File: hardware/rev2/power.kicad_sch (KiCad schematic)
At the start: 20 parts, among them U5 MP2664GG-xxxx-P, U6 TPS63805YFFR, U7 MAX17055ETB+

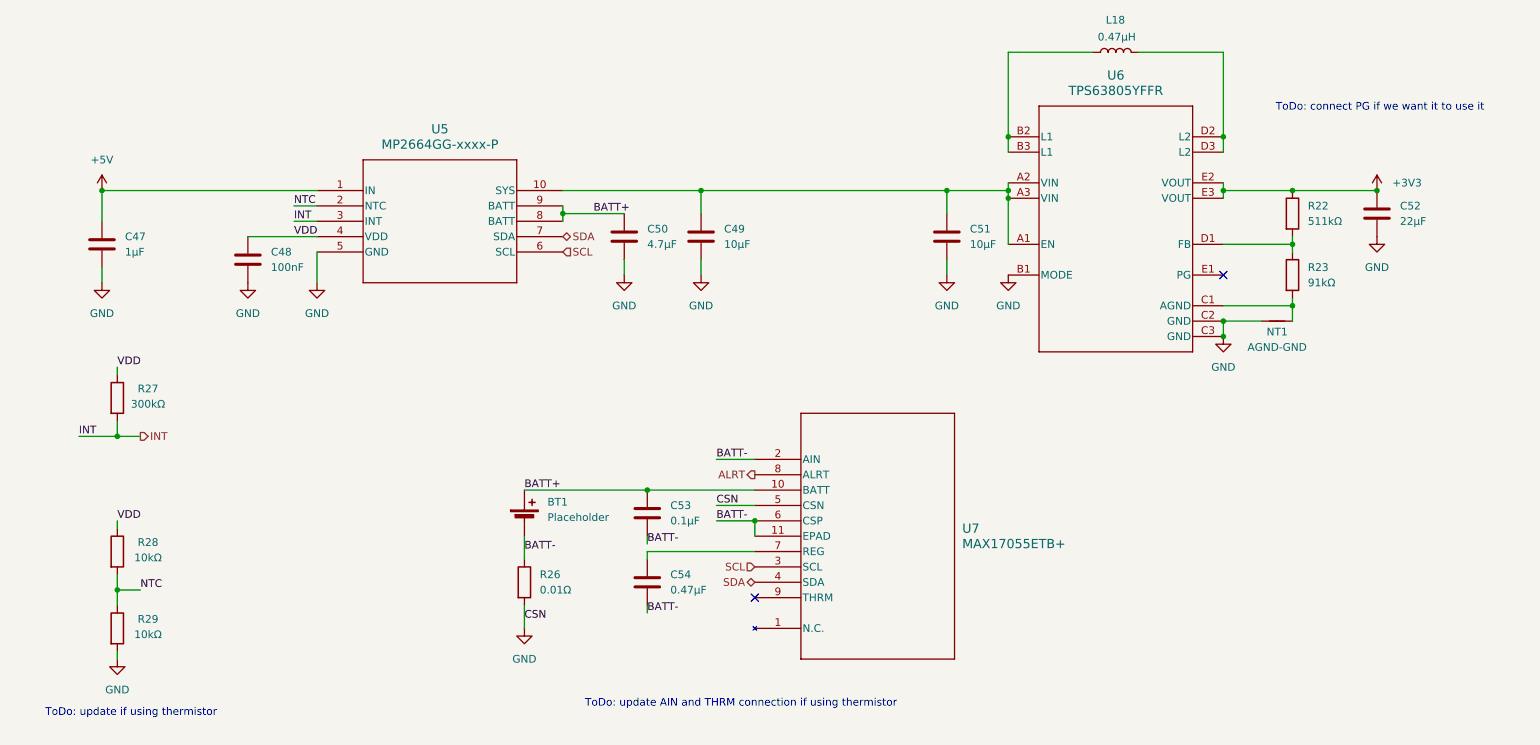
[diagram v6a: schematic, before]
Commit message: finished routing most of the RF and power for SX1262 and ESP32, also decided final ish positions for both.
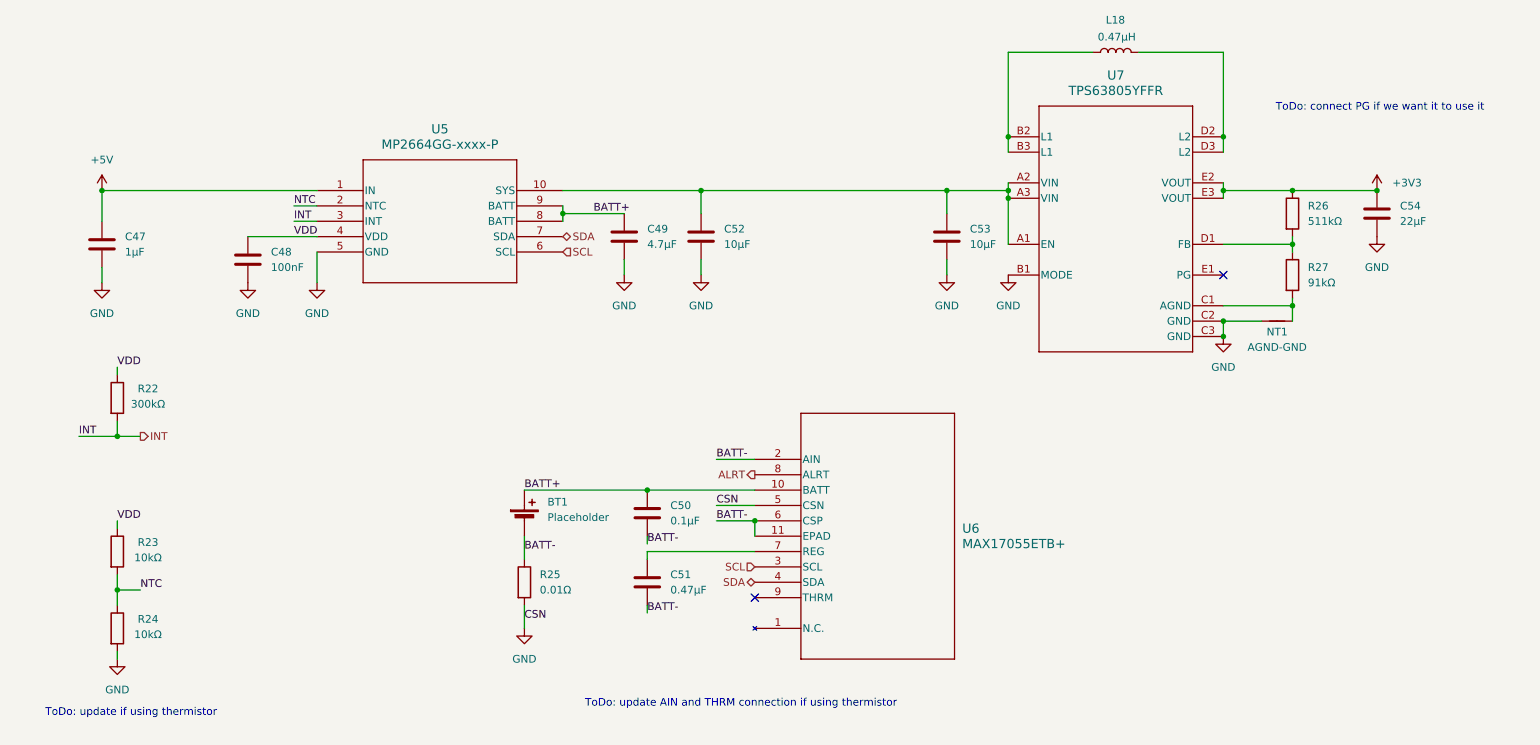
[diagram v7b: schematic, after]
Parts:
- renumbered C50 to C49, C53 to C50, C54 to C51, C49 to C52, C51 to C53, C52 to C54, R27 to R22, R28 to R23, R29 to R24, R26 to R25, R22 to R26, R23 to R27, U7 to U6, U6 to U7
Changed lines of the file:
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@@
 		(dnp no)
 		(fields_autoplaced yes)
-		(property "Reference" "#PWR072"
+		(property "Reference" "#PWR075"
 			(at 53.34 96.52 0)
 			(hide yes)
@@
 			(project "rev2"
 				(path "/9067f306-e23c-4d77-8182-4fa2c4b88902/46484475-7656-401a-9d45-159f5e421427"
-					(reference "#PWR072")
+					(reference "#PWR075")
 					(unit 1)
 				)
@@
 		(dnp no)
 		(fields_autoplaced yes)
-		(property "Reference" "#PWR074"
+		(property "Reference" "#PWR078"
 			(at 115.57 95.25 0)
 			(hide yes)
@@
 			(project "rev2"
 				(path "/9067f306-e23c-4d77-8182-4fa2c4b88902/46484475-7656-401a-9d45-159f5e421427"
-					(reference "#PWR074")
+					(reference "#PWR078")
 					(unit 1)
 				)
@@
 		(dnp no)
 		(fields_autoplaced yes)
-		(property "Reference" "#PWR076"
+		(property "Reference" "#PWR079"
 			(at 128.27 95.25 0)
 			(hide yes)
@@
 			(project "rev2"
 				(path "/9067f306-e23c-4d77-8182-4fa2c4b88902/46484475-7656-401a-9d45-159f5e421427"
-					(reference "#PWR076")
+					(reference "#PWR079")
 					(unit 1)
 				)
@@
 		(dnp no)
 		(fields_autoplaced yes)
-		(property "Reference" "C51"
+		(property "Reference" "C53"
 			(at 172.72 81.2799 0)
 			(show_name no)
@@
 			(project "rev2"
 				(path "/9067f306-e23c-4d77-8182-4fa2c4b88902/46484475-7656-401a-9d45-159f5e421427"
-					(reference "C51")
+					(reference "C53")
 					(unit 1)
 				)
@@
 		(dnp no)
 		(fields_autoplaced yes)
-		(property "Reference" "#PWR071"
+		(property "Reference" "#PWR073"
 			(at 29.21 96.52 0)
 			(hide yes)
@@
 			(project "rev2"
 				(path "/9067f306-e23c-4d77-8182-4fa2c4b88902/46484475-7656-401a-9d45-159f5e421427"
-					(reference "#PWR071")
+					(reference "#PWR073")
 					(unit 1)
 				)
@@
 		(in_pos_files yes)
 		(dnp no)
-		(property "Reference" "R28"
+		(property "Reference" "R23"
 			(at 36.83 133.096 0)
 			(show_name no)
@@
 			(project "rev2"
 				(path "/9067f306-e23c-4d77-8182-4fa2c4b88902/46484475-7656-401a-9d45-159f5e421427"
-					(reference "R28")
+					(reference "R23")
 					(unit 1)
 				)
@@
 		(dnp no)
 		(fields_autoplaced yes)
-		(property "Reference" "#PWR077"
+		(property "Reference" "#PWR080"
 			(at 168.91 95.25 0)
 			(hide yes)
@@
 			(project "rev2"
 				(path "/9067f306-e23c-4d77-8182-4fa2c4b88902/46484475-7656-401a-9d45-159f5e421427"
-					(reference "#PWR077")
+					(reference "#PWR080")
 					(unit 1)
 				)
@@
 		(in_pos_files yes)
 		(dnp no)
-		(property "Reference" "C54"
+		(property "Reference" "C51"
 			(at 123.19 138.4299 0)
 			(show_name no)
@@
 			(project "rev2"
 				(path "/9067f306-e23c-4d77-8182-4fa2c4b88902/46484475-7656-401a-9d45-159f5e421427"
-					(reference "C54")
+					(reference "C51")
 					(unit 1)
 				)
@@
 		(dnp no)
 		(fields_autoplaced yes)
-		(property "Reference" "#PWR080"
+		(property "Reference" "#PWR084"
 			(at 240.03 88.9 0)
 			(hide yes)
@@
 			(project "rev2"
 				(path "/9067f306-e23c-4d77-8182-4fa2c4b88902/46484475-7656-401a-9d45-159f5e421427"
-					(reference "#PWR080")
+					(reference "#PWR084")
 					(unit 1)
 				)
@@
 		(dnp no)
 		(fields_autoplaced yes)
-		(property "Reference" "C52"
+		(property "Reference" "C54"
 			(at 243.84 77.4699 0)
 			(show_name no)
@@
 			(project "rev2"
 				(path "/9067f306-e23c-4d77-8182-4fa2c4b88902/46484475-7656-401a-9d45-159f5e421427"
-					(reference "C52")
+					(reference "C54")
 					(unit 1)
 				)
@@
 		(dnp no)
 		(fields_autoplaced yes)
-		(property "Reference" "R22"
+		(property "Reference" "R26"
 			(at 228.6 77.4699 0)
 			(show_name no)
@@
 			(project "rev2"
 				(path "/9067f306-e23c-4d77-8182-4fa2c4b88902/46484475-7656-401a-9d45-159f5e421427"
-					(reference "R22")
+					(reference "R26")
 					(unit 1)
 				)
@@
 		(dnp no)
 		(fields_autoplaced yes)
-		(property "Reference" "U6"
+		(property "Reference" "U7"
 			(at 196.85 55.88 0)
 			(show_name no)
@@
 			(project "rev2"
 				(path "/9067f306-e23c-4d77-8182-4fa2c4b88902/46484475-7656-401a-9d45-159f5e421427"
-					(reference "U6")
+					(reference "U7")
 					(unit 1)
 				)
@@
 		(dnp no)
 		(fields_autoplaced yes)
-		(property "Reference" "C50"
+		(property "Reference" "C49"
 			(at 119.38 81.2799 0)
 			(show_name no)
@@
 			(project "rev2"
 				(path "/9067f306-e23c-4d77-8182-4fa2c4b88902/46484475-7656-401a-9d45-159f5e421427"
-					(reference "C50")
+					(reference "C49")
 					(unit 1)
 				)
@@
 		(dnp no)
 		(fields_autoplaced yes)
-		(property "Reference" "U7"
+		(property "Reference" "U6"
 			(at 171.45 130.8099 0)
 			(show_name no)
@@
 			(project "rev2"
 				(path "/9067f306-e23c-4d77-8182-4fa2c4b88902/46484475-7656-401a-9d45-159f5e421427"
-					(reference "U7")
+					(reference "U6")
 					(unit 1)
 				)
@@
 		(dnp no)
 		(fields_autoplaced yes)
-		(property "Reference" "C53"
+		(property "Reference" "C50"
 			(at 123.19 126.9999 0)
 			(show_name no)
@@
 			(project "rev2"
 				(path "/9067f306-e23c-4d77-8182-4fa2c4b88902/46484475-7656-401a-9d45-159f5e421427"
-					(reference "C53")
+					(reference "C50")
 					(unit 1)
 				)
@@
 		(in_pos_files yes)
 		(dnp no)
-		(property "Reference" "R27"
+		(property "Reference" "R22"
 			(at 36.83 107.696 0)
 			(show_name no)
@@
 			(project "rev2"
 				(path "/9067f306-e23c-4d77-8182-4fa2c4b88902/46484475-7656-401a-9d45-159f5e421427"
-					(reference "R27")
+					(reference "R22")
 					(unit 1)
 				)
@@
 		(dnp no)
 		(fields_autoplaced yes)
-		(property "Reference" "#PWR075"
+		(property "Reference" "#PWR077"
 			(at 99.06 153.67 0)
 			(hide yes)
@@
 			(project "rev2"
 				(path "/9067f306-e23c-4d77-8182-4fa2c4b88902/46484475-7656-401a-9d45-159f5e421427"
-					(reference "#PWR075")
+					(reference "#PWR077")
 					(unit 1)
 				)
@@
 		(in_pos_files yes)
 		(dnp no)
-		(property "Reference" "R29"
+		(property "Reference" "R24"
 			(at 36.83 145.796 0)
 			(show_name no)
@@
 			(project "rev2"
 				(path "/9067f306-e23c-4d77-8182-4fa2c4b88902/46484475-7656-401a-9d45-159f5e421427"
-					(reference "R29")
+					(reference "R24")
 					(unit 1)
 				)
@@
 		(dnp no)
 		(fields_autoplaced yes)
-		(property "Reference" "C49"
+		(property "Reference" "C52"
 			(at 132.08 81.2799 0)
 			(show_name no)
@@
 			(project "rev2"
 				(path "/9067f306-e23c-4d77-8182-4fa2c4b88902/46484475-7656-401a-9d45-159f5e421427"
-					(reference "C49")
+					(reference "C52")
 					(unit 1)
 				)
@@
 		(dnp no)
 		(fields_autoplaced yes)
-		(property "Reference" "#PWR079"
+		(property "Reference" "#PWR082"
 			(at 214.63 105.41 0)
 			(hide yes)
@@
 			(project "rev2"
 				(path "/9067f306-e23c-4d77-8182-4fa2c4b88902/46484475-7656-401a-9d45-159f5e421427"
-					(reference "#PWR079")
+					(reference "#PWR082")
 					(unit 1)
 				)
@@
 		(dnp no)
 		(fields_autoplaced yes)
-		(property "Reference" "#PWR073"
+		(property "Reference" "#PWR076"
 			(at 64.77 96.52 0)
 			(hide yes)
@@
 			(project "rev2"
 				(path "/9067f306-e23c-4d77-8182-4fa2c4b88902/46484475-7656-401a-9d45-159f5e421427"
-					(reference "#PWR073")
+					(reference "#PWR076")
 					(unit 1)
 				)
@@
 		(dnp no)
 		(fields_autoplaced yes)
-		(property "Reference" "#PWR082"
+		(property "Reference" "#PWR072"
 			(at 29.21 78.74 0)
 			(hide yes)
@@
 			(project "rev2"
 				(path "/9067f306-e23c-4d77-8182-4fa2c4b88902/46484475-7656-401a-9d45-159f5e421427"
-					(reference "#PWR082")
+					(reference "#PWR072")
 					(unit 1)
 				)
@@
 		(dnp no)
 		(fields_autoplaced yes)
-		(property "Reference" "#PWR083"
+		(property "Reference" "#PWR074"
 			(at 31.75 158.75 0)
 			(hide yes)
@@
 			(project "rev2"
 				(path "/9067f306-e23c-4d77-8182-4fa2c4b88902/46484475-7656-401a-9d45-159f5e421427"
-					(reference "#PWR083")
+					(reference "#PWR074")
 					(unit 1)
 				)
@@
 		(dnp no)
 		(fields_autoplaced yes)
-		(property "Reference" "#PWR081"
+		(property "Reference" "#PWR083"
 			(at 240.03 78.74 0)
 			(hide yes)
@@
 			(project "rev2"
 				(path "/9067f306-e23c-4d77-8182-4fa2c4b88902/46484475-7656-401a-9d45-159f5e421427"
-					(reference "#PWR081")
+					(reference "#PWR083")
 					(unit 1)
 				)
@@
 		(dnp no)
 		(fields_autoplaced yes)
-		(property "Reference" "#PWR078"
+		(property "Reference" "#PWR081"
 			(at 179.07 95.25 0)
 			(hide yes)
@@
 			(project "rev2"
 				(path "/9067f306-e23c-4d77-8182-4fa2c4b88902/46484475-7656-401a-9d45-159f5e421427"
-					(reference "#PWR078")
+					(reference "#PWR081")
 					(unit 1)
 				)
@@
 		(dnp no)
 		(fields_autoplaced yes)
-		(property "Reference" "R23"
+		(property "Reference" "R27"
 			(at 228.6 87.6299 0)
 			(show_name no)
@@
 			(project "rev2"
 				(path "/9067f306-e23c-4d77-8182-4fa2c4b88902/46484475-7656-401a-9d45-159f5e421427"
-					(reference "R23")
+					(reference "R27")
 					(unit 1)
 				)
@@
 		(dnp no)
 		(fields_autoplaced yes)
-		(property "Reference" "R26"
+		(property "Reference" "R25"
 			(at 101.6 138.4299 0)
 			(show_name no)
@@
 			(project "rev2"
 				(path "/9067f306-e23c-4d77-8182-4fa2c4b88902/46484475-7656-401a-9d45-159f5e421427"
-					(reference "R26")
-					(unit 1)
-				)
+					(reference "R25")
+					(unit 1)
+				)
